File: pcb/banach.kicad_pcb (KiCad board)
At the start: 2 copper layers, 133.7 x 90.8 mm, 65 parts, among them J1 MJ-4PP-9, J2 OLED, SW10 SW_PUSH, SW11 SW_PUSH, SW12 SW_PUSH, SW14 SW_PUSH, SW15 SW_PUSH, SW16 SW_PUSH, SW17 SW_PUSH, SW18 SW_PUSH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

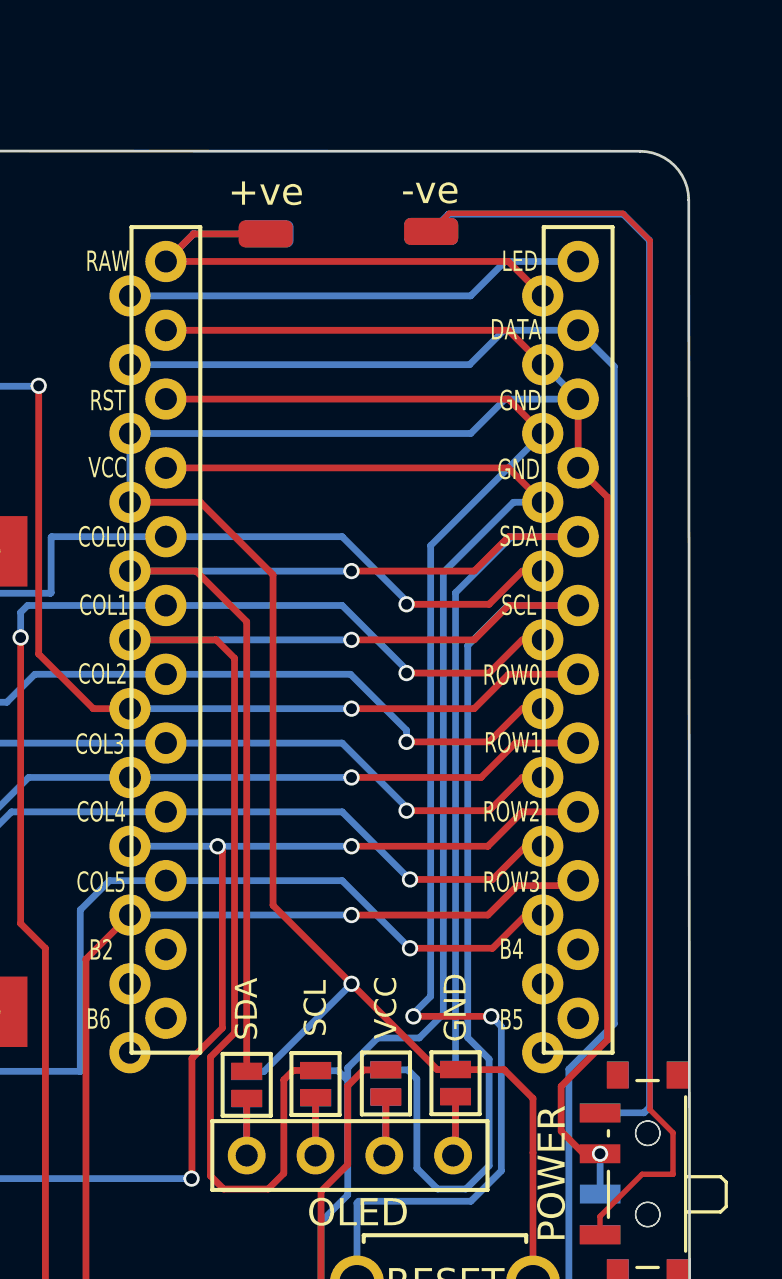
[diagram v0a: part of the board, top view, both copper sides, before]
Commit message: rotated battery pads 90 degrees
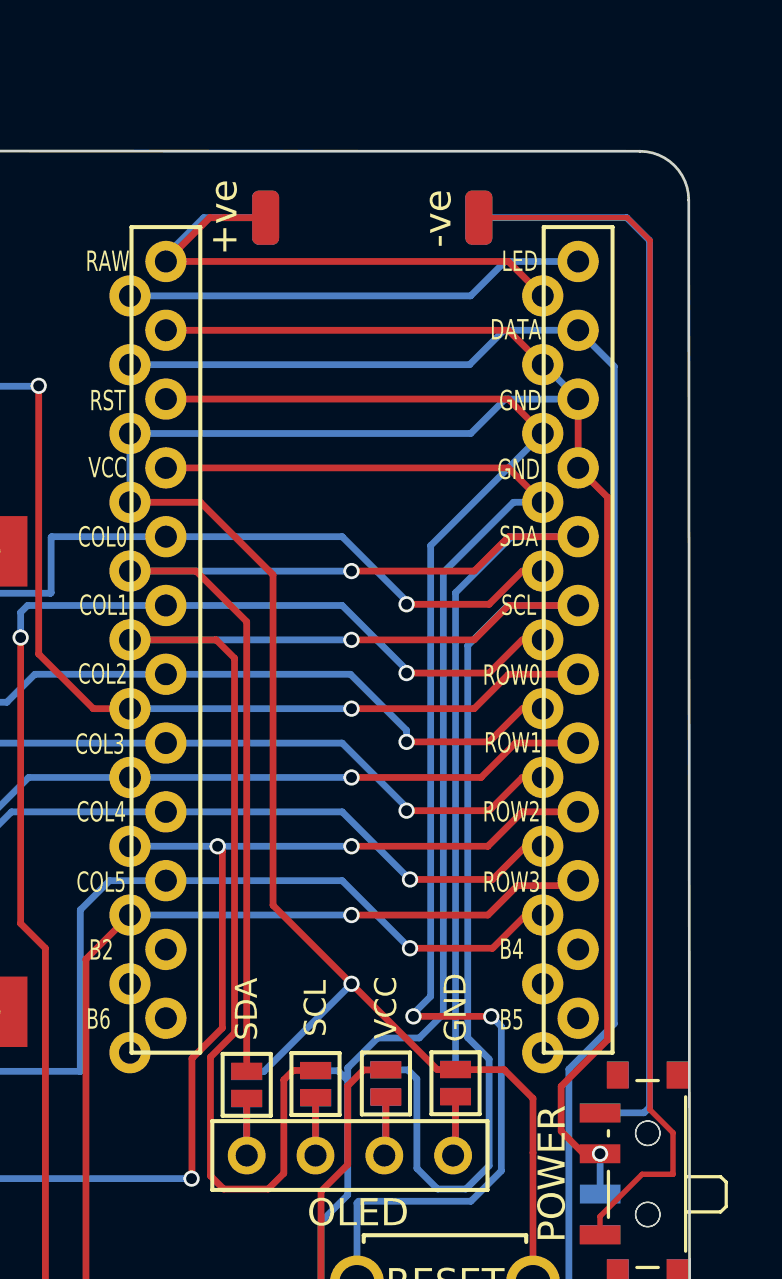
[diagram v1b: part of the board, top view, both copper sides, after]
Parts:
- moved -ve 1.83 mm to (184.2, 52.8), turned to 0 degrees (x2)
- moved +ve 0.60 mm to (176.3, 52.8), turned to 0 degrees
- moved +ve 0.60 mm to (176.3, 52.8), turned to 180 degrees
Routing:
- net (no net): track 195.9 -> 187.1 mm
- net Net-(U1-Pad24): track 22.7 -> 27.8 mm
